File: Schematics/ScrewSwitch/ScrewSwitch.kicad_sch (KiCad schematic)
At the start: 4 parts, among them J1 Mount, J2 BottomPad, J3 TopPad, J4 Mount

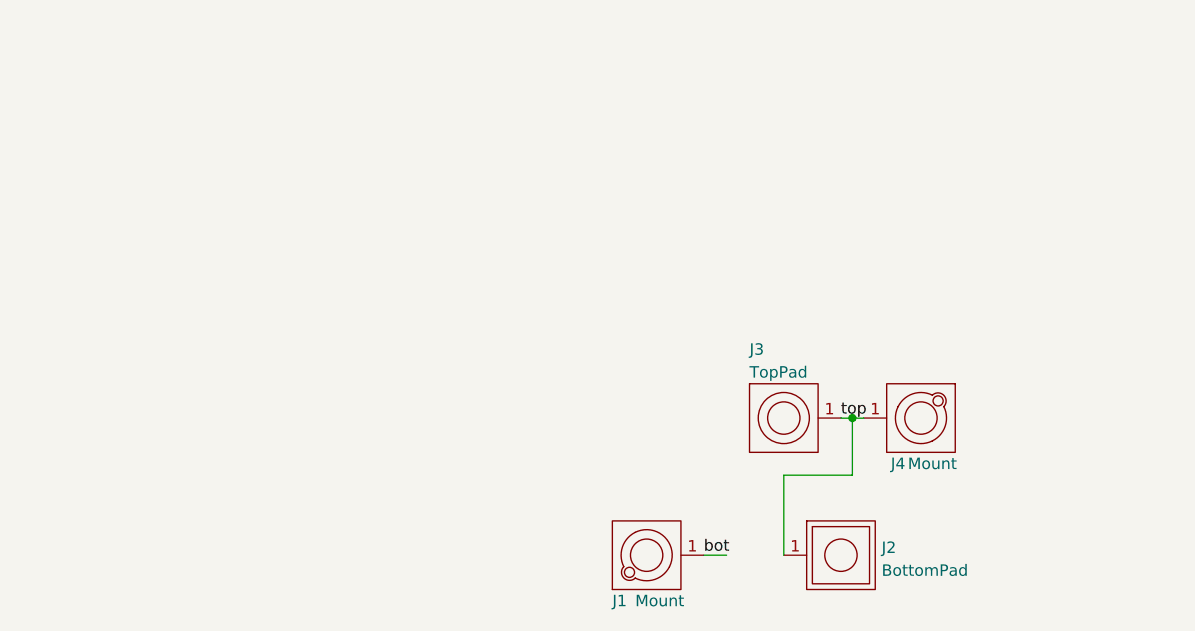
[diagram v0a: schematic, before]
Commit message: Finished draft of screw switch PCB
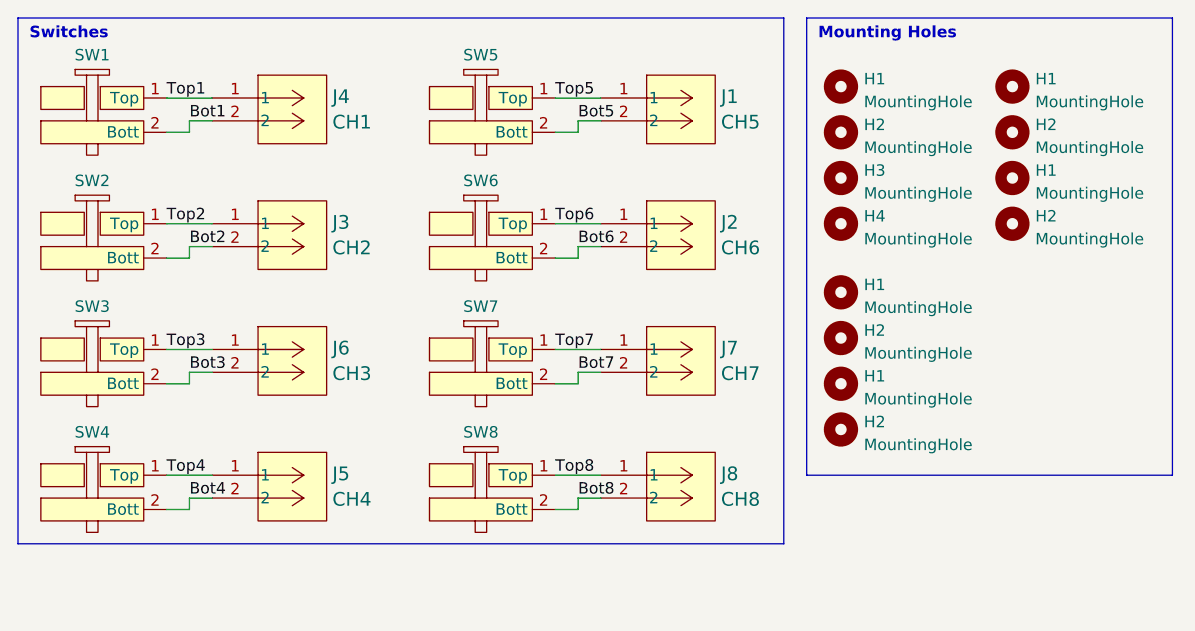
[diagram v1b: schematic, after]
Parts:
- removed J1, J4: Mount, ScrewSwitchLibrary:ScrewTermMount, symbol ScrewSwitchSymbols:Mount
- removed J2: BottomPad, ScrewSwitchLibrary:ScrewTermBack, symbol ScrewSwitchSymbols:BottomPad
- removed J3: TopPad, ScrewSwitchLibrary:ScrewTermFront, symbol ScrewSwitchSymbols:TopPad
- added H1 (x5), H2 (x5), H3, H4: MountingHole, MountingHole:MountingHole_3.2mm_M3_ISO14580_Pad, symbol Mechanical:MountingHole
- added J1: CH5, footprints:CONN_2-1445057-2_TYCO, symbol CONN_2-1445057-2_TYCO:2-1445057-2
- added J2: CH6, footprints:CONN_2-1445057-2_TYCO, symbol CONN_2-1445057-2_TYCO:2-1445057-2
- added J3: CH2, footprints:CONN_2-1445057-2_TYCO, symbol CONN_2-1445057-2_TYCO:2-1445057-2
- added J4: CH1, footprints:CONN_2-1445057-2_TYCO, symbol CONN_2-1445057-2_TYCO:2-1445057-2
- added J5: CH4, footprints:CONN_2-1445057-2_TYCO, symbol CONN_2-1445057-2_TYCO:2-1445057-2
- added J6: CH3, footprints:CONN_2-1445057-2_TYCO, symbol CONN_2-1445057-2_TYCO:2-1445057-2
- added J7: CH7, footprints:CONN_2-1445057-2_TYCO, symbol CONN_2-1445057-2_TYCO:2-1445057-2
- added J8: CH8, footprints:CONN_2-1445057-2_TYCO, symbol CONN_2-1445057-2_TYCO:2-1445057-2
- added SW1, SW2, SW3, SW4, SW5, SW6, SW7, SW8: ~, ScrewSwitchLibrary:ScrewSwitchNew, symbol ScrewSwitchSymbols:ScrewSwitch
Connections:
- new net Bot1: J4.2, SW1.2 (Bott)
- new net Bot2: J3.2, SW2.2 (Bott)
- new net Bot3: J6.2, SW3.2 (Bott)
- new net Bot4: J5.2, SW4.2 (Bott)
- new net Bot5: J1.2, SW5.2 (Bott)
- new net Bot6: J2.2, SW6.2 (Bott)
- new net Bot7: J7.2, SW7.2 (Bott)
- new net Bot8: J8.2, SW8.2 (Bott)
- new net Top1: J4.1, SW1.1 (Top)
- new net Top2: J3.1, SW2.1 (Top)
- new net Top3: J6.1, SW3.1 (Top)
- new net Top4: J5.1, SW4.1 (Top)
- new net Top5: J1.1, SW5.1 (Top)
- new net Top6: J2.1, SW6.1 (Top)
- new net Top7: J7.1, SW7.1 (Top)
- new net Top8: J8.1, SW8.1 (Top)
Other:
- note added: "Mounting Holes"
- note added: "Switches"
- title: QRET Screw Switch -> QRET Screw Switch PCB (2025)
